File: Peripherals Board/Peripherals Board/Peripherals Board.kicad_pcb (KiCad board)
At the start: 2 copper layers, 14 parts

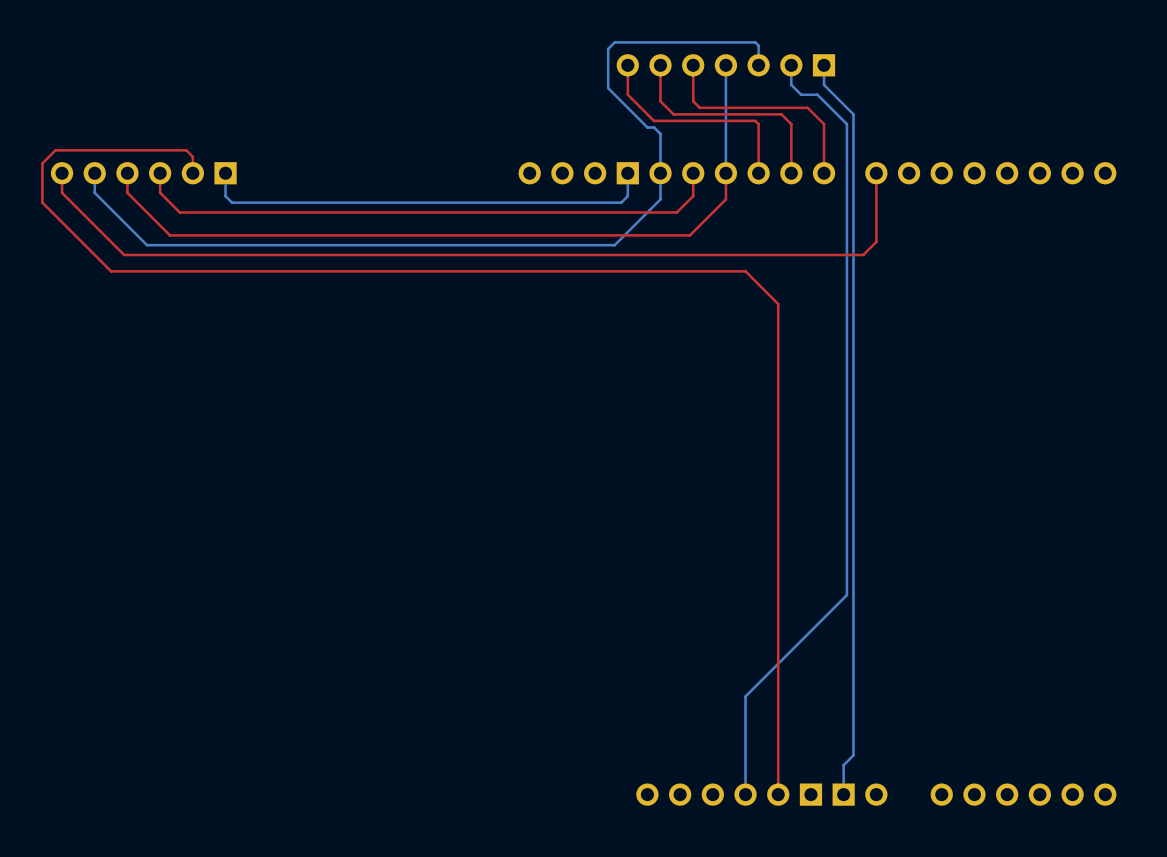
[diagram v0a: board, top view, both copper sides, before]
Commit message: added PBs to PCB and changed PB definitions to be reversed to accomodate PCB better
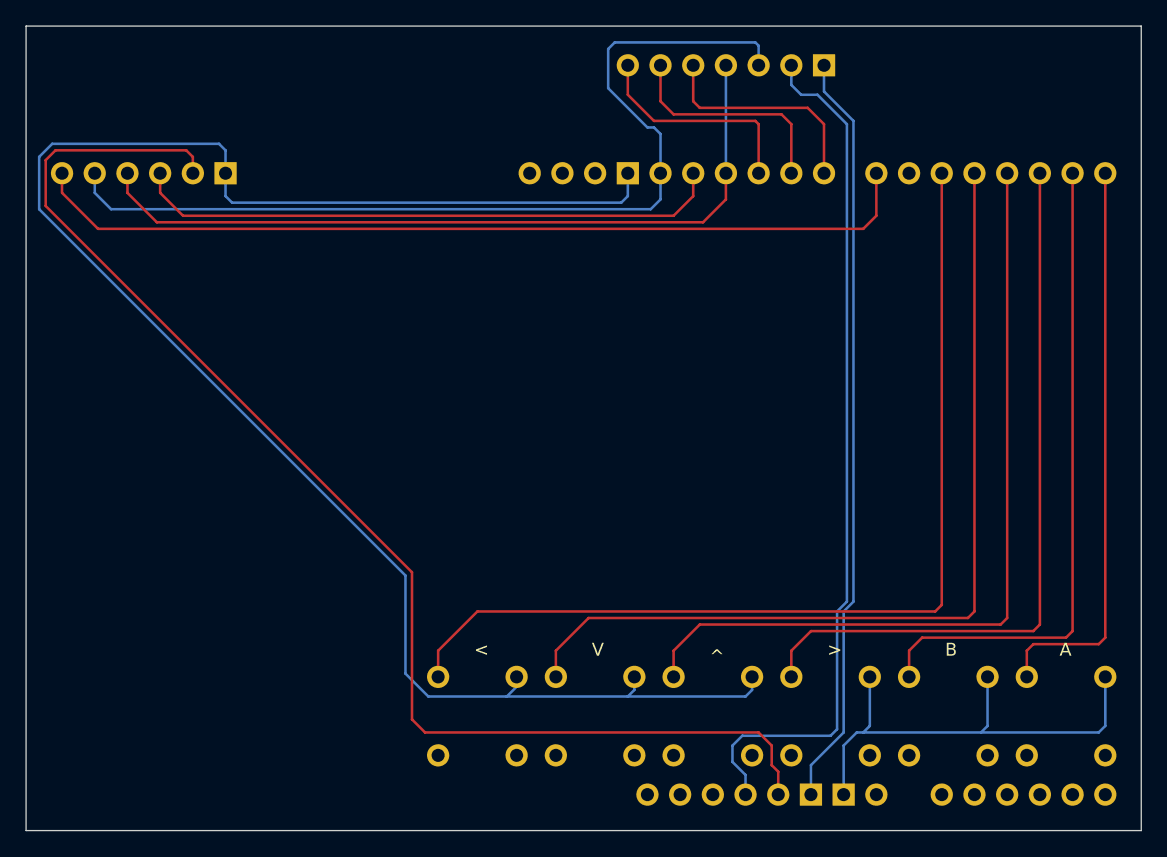
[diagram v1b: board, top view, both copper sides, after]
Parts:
- added ?: , , F.Cu at (165.1, 117.9)
- added ?: , , F.Cu at (128.5, 124.0)
- added ?: , , F.Cu at (165.1, 124.0)
- added ?: , , F.Cu at (134.6, 117.9)
- added ?: , , F.Cu at (146.8, 124.0)
- added ?: , , F.Cu at (171.2, 117.9)
- added ?: , , F.Cu at (137.7, 117.9)
- added ?: , , F.Cu at (171.2, 124.0)
- added ?: , , F.Cu at (146.8, 117.9)
- added ?: , , F.Cu at (180.3, 117.9)
- added ?: , , F.Cu at (134.6, 124.0)
- added ?: , , F.Cu at (162.1, 124.0)
- added ?: , , F.Cu at (128.5, 117.9)
- added ?: , , F.Cu at (152.9, 117.9)
- added ?: , , F.Cu at (156.0, 117.9)
- added ?: , , F.Cu at (162.1, 117.9)
- added ?: , , F.Cu at (143.8, 117.9)
- added ?: , , F.Cu at (143.8, 124.0)
- added ?: , , F.Cu at (156.0, 124.0)
- added ?: , , F.Cu at (180.3, 124.0)
- added ?: , , F.Cu at (152.9, 124.0)
- added ?: , , F.Cu at (174.2, 124.0)
- added ?: , , F.Cu at (137.7, 124.0)
- added ?: , , F.Cu at (174.2, 117.9)
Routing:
- net (no net): track 578.3 -> 1065.7 mm
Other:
- board outline added: 86.6 x 62.5 mm
- board text added: "<"
- board text added: ">"
- board text added: "A"
- board text added: "B"
- board text added: "V"
- board text added: "^"
